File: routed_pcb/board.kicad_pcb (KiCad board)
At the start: 2 copper layers, 100 x 100 mm, 31 parts

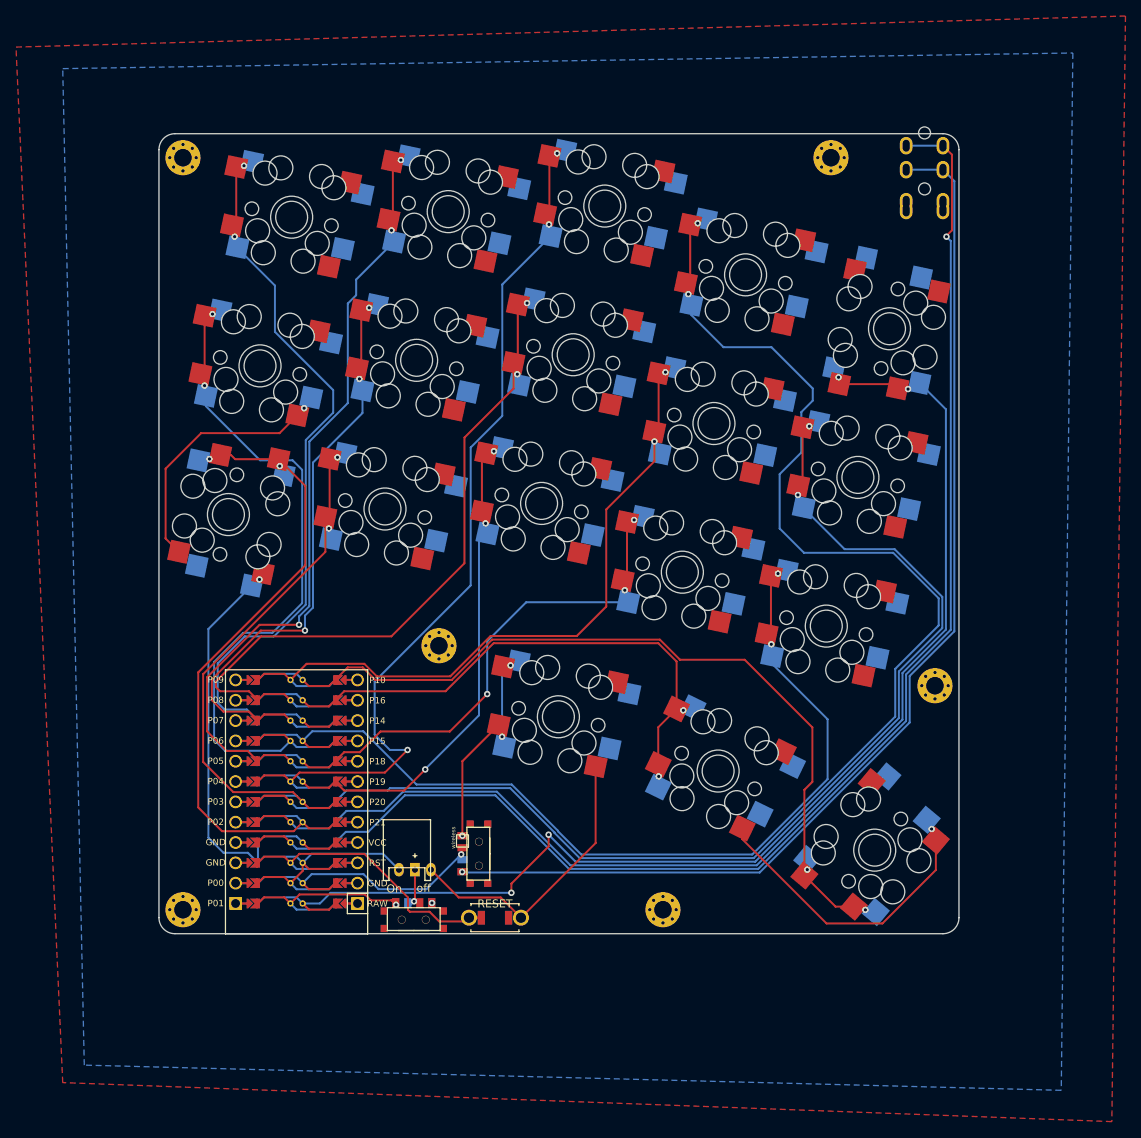
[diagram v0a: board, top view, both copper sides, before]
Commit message: updated images, moved output pcb to routed (not actually routed yet)
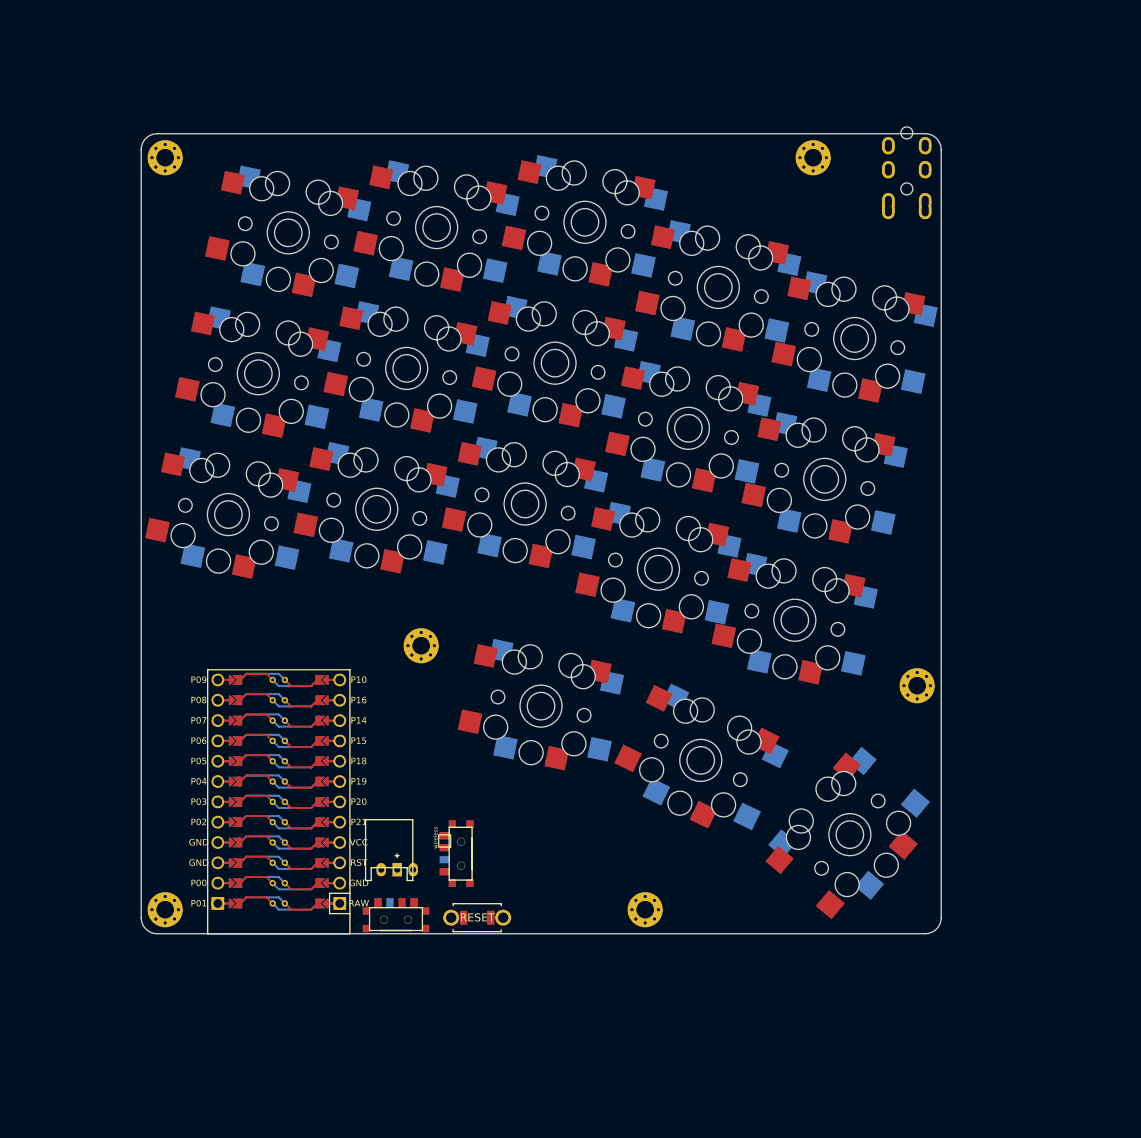
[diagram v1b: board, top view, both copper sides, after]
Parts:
- B1, B2, JST1, MCU1, SW1, SW10, SW11, SW12, SW13, SW14, SW15, SW16, SW17, SW18, SW2, SW3, SW4, SW5, SW6, SW7, SW8, SW9, T1, T2: value ~ -> (none)
- moved SW15 4.52 mm to (155.3, 96.6), turned to -12 degrees
- moved SW14 4.15 mm to (151.6, 114.2)
- moved SW13 4.00 mm to (147.8, 131.8)
- moved SW12 3.75 mm to (138.3, 90.2)
- moved SW18 3.66 mm to (154.7, 158.6)
- moved SW11 3.25 mm to (134.5, 107.8)
- moved SW9 3.20 mm to (121.6, 82.1)
- moved SW10 3.01 mm to (130.8, 125.4)
- moved SW17 2.55 mm to (136.1, 149.3)
- moved SW16 2.55 mm to (116.1, 142.6)
- moved SW8 2.50 mm to (117.9, 99.7)
- moved SW6 2.46 mm to (103.1, 82.7)
- moved MCU1 2.22 mm to (83.3, 153.2)
- moved B1 2.22 mm to (108.1, 169.0)
- moved B2 2.22 mm to (108.1, 169.0), turned to 0 degrees
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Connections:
- net /Bplus renamed Bplus
- net /GND renamed GND
- net /P0 renamed P0
- net /RAW renamed RAW
- net /RST renamed RST
- net /VCC renamed VCC
- net /matrix_index_bottom renamed matrix_index_bottom
- net /matrix_index_home renamed matrix_index_home
- net /matrix_index_top renamed matrix_index_top
- net /matrix_inner_bottom renamed matrix_inner_bottom
- net /matrix_inner_home renamed matrix_inner_home
- net /matrix_inner_top renamed matrix_inner_top
- net /matrix_middle_bottom renamed matrix_middle_bottom
- net /matrix_middle_home renamed matrix_middle_home
- net /matrix_middle_top renamed matrix_middle_top
- net /matrix_pinky_bottom renamed matrix_pinky_bottom
- net /matrix_pinky_home renamed matrix_pinky_home
- net /matrix_pinky_top renamed matrix_pinky_top
- net /matrix_ring_bottom renamed matrix_ring_bottom
- net /matrix_ring_home renamed matrix_ring_home
- net /matrix_ring_top renamed matrix_ring_top
- net /thumb_inner renamed thumb_inner
- net /thumb_reachy renamed thumb_reachy
- net /thumb_tucky renamed thumb_tucky
- net /trrs_data renamed trrs_data
- T1 pad 3: unconnected-(T1-C-Pad3) -> (no net)
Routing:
- net matrix_index_top: track 174.5 -> 0.00 mm, vias 2 -> 0
- net GND: track 169.6 -> 0.00 mm, vias 3 -> 0
- net VCC: track 165.2 -> 0.00 mm, vias 1 -> 0
- net matrix_inner_top: track 142.4 -> 0.00 mm, vias 2 -> 0
- net matrix_inner_home: track 140.7 -> 0.00 mm, vias 4 -> 0
- net trrs_data: track 140.4 -> 0.00 mm, vias 1 -> 0
- net matrix_inner_bottom: track 107.5 -> 0.00 mm, vias 2 -> 0
- net matrix_middle_top: track 105.4 -> 0.00 mm, vias 3 -> 0
- net thumb_reachy: track 99.5 -> 0.00 mm, vias 2 -> 0
- net matrix_ring_top: track 94.5 -> 0.00 mm, vias 3 -> 0
- net matrix_pinky_top: track 88.8 -> 0.00 mm, vias 2 -> 0
- net matrix_middle_home: track 84.2 -> 0.00 mm, vias 2 -> 0
- net matrix_index_home: track 80.5 -> 0.00 mm, vias 2 -> 0
- net matrix_pinky_home: track 80.5 -> 0.00 mm, vias 2 -> 0
- net matrix_pinky_bottom: track 78.0 -> 0.00 mm, vias 2 -> 0
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- removed copper zone on B.Cu, net GND
- removed copper zone on F.Cu, net GND
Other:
- net class Default added: clearance 0.2, trace_width 0.25, via_dia 0.8, via_drill 0.4
- board text removed: "On"
- board text removed: "off"
